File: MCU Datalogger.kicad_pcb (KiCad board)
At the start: 2 copper layers, 51.4 x 34.3 mm, 31 parts, among them J1 Conn_01x04_Male, J2 Conn_01x09_Male, J3 Conn_01x04_Male, J4 Conn_02x03_Odd_Even, U1 24LC1025, U2 DS1337S+, U3 24LC1025, U4 ATMEGA328P-AU, Y1 32.768 KHz, Y2 16 MHz

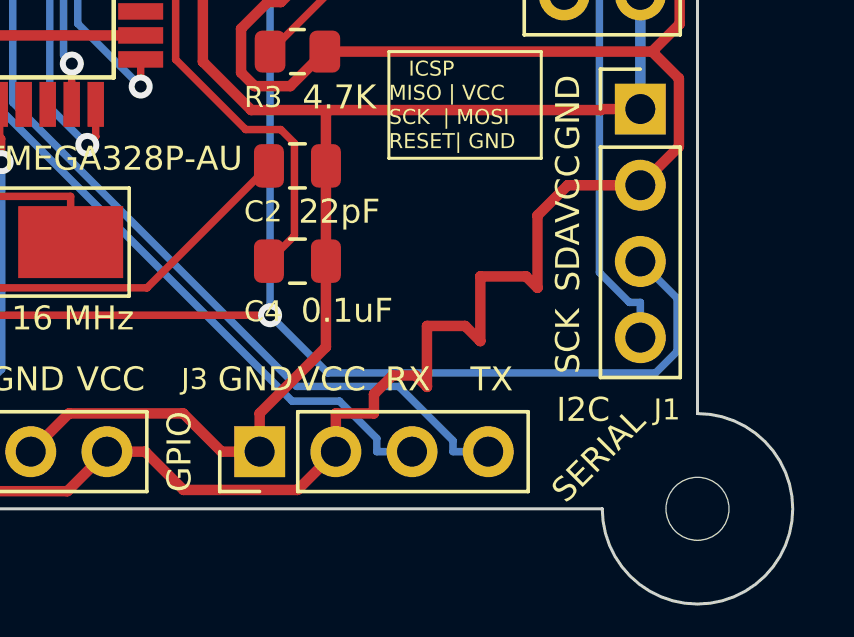
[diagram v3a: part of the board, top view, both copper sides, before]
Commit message: Changes due to various feature demos.
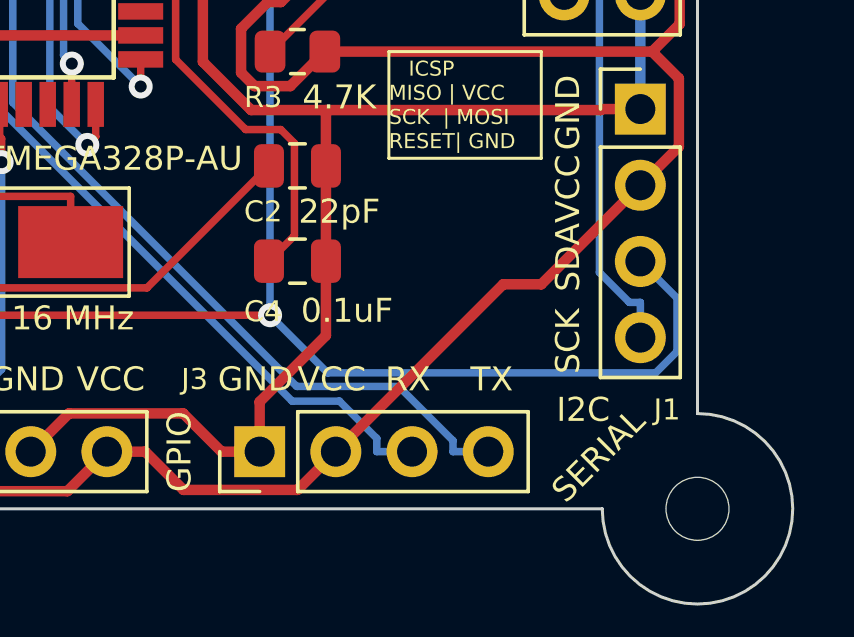
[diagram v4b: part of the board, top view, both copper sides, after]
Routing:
- net /Vcc: track 189.0 -> 182.9 mm
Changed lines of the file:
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@@
   (segment (start 111.9753 84.69) (end 117.4247 84.69) (width 0.35) (layer "F.Cu") (net 1))
   (segment (start 107.6152 85.49) (end 110 85.49) (width 0.35) (layer "F.Cu") (net 1))
-  (segment (start 124.775 94.615) (end 124.775 97.4797) (width 0.35) (layer "F.Cu") (net 1))
   (segment (start 110.7217 76.7517) (end 111.3752 76.7517) (width 0.35) (layer "F.Cu") (net 1))
   (segment (start 114.935 100.965) (end 116.2103 99.6897) (width 0.35) (layer "F.Cu") (net 1))
@@
   (segment (start 123.5904 81.1571) (end 124.7375 80.01) (width 0.35) (layer "F.Cu") (net 1))
   (segment (start 119.695 77.8868) (end 119.695 78.5117) (width 0.35) (layer "F.Cu") (net 1))
+  (segment (start 124.775 97.094) (end 124.775 94.615) (width 0.35) (layer "F.Cu") (net 1))
   (segment (start 133.9454 89.5793) (end 124.775 89.5793) (width 0.35) (layer "F.Cu") (net 1))
   (segment (start 106.7068 84.5816) (end 105.3266 84.5816) (width 0.35) (layer "F.Cu") (net 1))
@@
   (segment (start 118.6 84.69) (end 119.7753 84.69) (width 0.35) (layer "F.Cu") (net 1))
   (segment (start 99.3951 78.0591) (end 98.806 77.47) (width 0.35) (layer "F.Cu") (net 1))
-  (segment (start 122.565 100.965) (end 122.565 99.6897) (width 0.35) (layer "F.Cu") (net 1))
   (segment (start 110 83.89) (end 111.1753 83.89) (width 0.35) (layer "F.Cu") (net 1))
+  (segment (start 122.565 100.965) (end 122.565 99.304) (width 0.35) (layer "F.Cu") (net 1))
   (segment (start 93.98 85.085) (end 95.2553 85.085) (width 0.35) (layer "F.Cu") (net 1))
   (segment (start 116.2103 99.6897) (end 120.0144 99.6897) (width 0.35) (layer "F.Cu") (net 1))
-  (segment (start 124.775 97.4797) (end 122.565 99.6897) (width 0.35) (layer "F.Cu") (net 1))
   (segment (start 100.1112 77.47) (end 105.2 77.47) (width 0.35) (layer "F.Cu") (net 1))
   (segment (start 119.695 76.2) (end 119.695 77.8868) (width 0.35) (layer "F.Cu") (net 1))
@@
   (segment (start 119.695 78.5117) (end 122.3404 81.1571) (width 0.35) (layer "F.Cu") (net 1))
   (segment (start 118.6 84.69) (end 117.4247 84.69) (width 0.35) (layer "F.Cu") (net 1))
+  (segment (start 122.565 99.304) (end 124.775 97.094) (width 0.35) (layer "F.Cu") (net 1))
   (segment (start 111.9269 76.2) (end 111.3752 76.7517) (width 0.35) (layer "F.Cu") (net 1))
   (segment (start 120.0144 99.6897) (end 121.2897 100.965) (width 0.35) (layer "F.Cu") (net 1))
@@
   (segment (start 128.5013 77.8868) (end 129.1825 78.568) (width 0.35) (layer "B.Cu") (net 1))
   (segment (start 93.98 82.545) (end 93.98 81.2697) (width 0.35) (layer "F.Cu") (net 2))
+  (segment (start 130.683 95.387) (end 131.953 95.387) (width 0.35) (layer "F.Cu") (net 2))
   (segment (start 105.2271 82.1769) (end 105.2271 83.1579) (width 0.35) (layer "F.Cu") (net 2))
   (segment (start 122.3954 88.7808) (end 121.9446 88.33) (width 0.35) (layer "F.Cu") (net 2))
@@
   (segment (start 124.7375 84.514) (end 124.7375 83.82) (width 0.35) (layer "F.Cu") (net 2))
   (segment (start 122.3831 82.0941) (end 123.0116 82.0941) (width 0.35) (layer "F.Cu") (net 2))
-  (segment (start 131.826 93.091) (end 132.832 92.085) (width 0.35) (layer "F.Cu") (net 2))
   (segment (start 105.2271 83.1579) (end 105.2 83.185) (width 0.35) (layer "F.Cu") (net 2))
-  (segment (start 127 98.425) (end 127.762 98.425) (width 0.35) (layer "F.Cu") (net 2))
-  (segment (start 128.143 98.806) (end 128.143 96.774) (width 0.35) (layer "F.Cu") (net 2))
   (segment (start 98 83.185) (end 95.8953 83.185) (width 0.35) (layer "F.Cu") (net 2))
   (segment (start 120.0257 102.2404) (end 123.8296 102.2404) (width 0.35) (layer "F.Cu") (net 2))
   (segment (start 103.2872 97.6503) (end 104.4175 96.52) (width 0.35) (layer "F.Cu") (net 2))
   (segment (start 98 85.725) (end 98 84.455) (width 0.35) (layer "F.Cu") (net 2))
-  (segment (start 128.143 96.774) (end 129.413 96.774) (width 0.35) (layer "F.Cu") (net 2))
   (segment (start 101.6 91.2347) (end 102.6647 90.17) (width 0.35) (layer "F.Cu") (net 2))
   (segment (start 124.7375 87.63) (end 123.5867 88.7808) (width 0.35) (layer "F.Cu") (net 2))
   (segment (start 102.6647 89.9899) (end 98.3998 85.725) (width 0.35) (layer "F.Cu") (net 2))
   (segment (start 118.7503 100.965) (end 120.0257 102.2404) (width 0.35) (layer "F.Cu") (net 2))
+  (segment (start 131.953 95.387) (end 135.255 92.085) (width 0.35) (layer "F.Cu") (net 2))
   (segment (start 97.645 76.2) (end 98 76.2) (width 0.35) (layer "F.Cu") (net 2))
   (segment (start 125.7262 80.6987) (end 125.7262 77.1637) (width 0.35) (layer "F.Cu") (net 2))
@@
   (segment (start 95.8403 99.9486) (end 95.8403 102.032) (width 0.35) (layer "F.Cu") (net 2))
   (segment (start 136.5396 90.8004) (end 136.5396 88.5225) (width 0.35) (layer "F.Cu") (net 2))
-  (segment (start 127.762 98.425) (end 128.143 98.806) (width 0.35) (layer "F.Cu") (net 2))
-  (segment (start 126.375 99.6897) (end 126.375 99.05) (width 0.35) (layer "F.Cu") (net 2))
   (segment (start 95.8403 102.032) (end 96.0919 102.2836) (width 0.35) (layer "F.Cu") (net 2))
   (segment (start 96.0919 102.2836) (end 116.1564 102.2836) (width 0.35) (layer "F.Cu") (net 2))
@@
   (segment (start 136.566 81.971) (end 136.566 86.7111) (width 0.35) (layer "F.Cu") (net 2))
   (segment (start 117.795 76.2) (end 117.795 77.506) (width 0.35) (layer "F.Cu") (net 2))
-  (segment (start 129.921 95.123) (end 131.445 95.123) (width 0.35) (layer "F.Cu") (net 2))
-  (segment (start 132.832 92.085) (end 135.255 92.085) (width 0.35) (layer "F.Cu") (net 2))
   (segment (start 106.5848 83.185) (end 108.0898 84.69) (width 0.35) (layer "F.Cu") (net 2))
   (segment (start 96.7226 78.74) (end 96.5097 78.74) (width 0.35) (layer "F.Cu") (net 2))
-  (segment (start 125.105 99.6897) (end 126.375 99.6897) (width 0.35) (layer "F.Cu") (net 2))
   (segment (start 101.6 97.6503) (end 101.6 91.2347) (width 0.35) (layer "F.Cu") (net 2))
   (segment (start 123.6712 82.7537) (end 124.7375 83.82) (width 0.35) (layer "F.Cu") (net 2))
+  (segment (start 125.105 100.965) (end 130.683 95.387) (width 0.35) (layer "F.Cu") (net 2))
   (segment (start 122.8345 85.9791) (end 123.2724 85.9791) (width 0.35) (layer "F.Cu") (net 2))
   (segment (start 102.6647 90.17) (end 102.6647 89.9899) (width 0.35) (layer "F.Cu") (net 2))
   (segment (start 127.3575 83.82) (end 124.7375 83.82) (width 0.35) (layer "F.Cu") (net 2))
-  (segment (start 129.413 96.774) (end 129.921 97.282) (width 0.35) (layer "F.Cu") (net 2))
   (segment (start 123.6712 82.7537) (end 125.7262 80.6987) (width 0.35) (layer "F.Cu") (net 2))
   (segment (start 98 84.455) (end 98 83.185) (width 0.35) (layer "F.Cu") (net 2))
-  (segment (start 131.445 95.123) (end 131.826 95.504) (width 0.35) (layer "F.Cu") (net 2))
   (segment (start 98.1427 97.6462) (end 95.8403 99.9486) (width 0.35) (layer "F.Cu") (net 2))
   (segment (start 95.8953 83.185) (end 95.2553 82.545) (width 0.35) (layer "F.Cu") (net 2))
   (segment (start 108.27 76.2) (end 105.2 76.2) (width 0.35) (layer "F.Cu") (net 2))
-  (segment (start 129.921 97.282) (end 129.921 95.123) (width 0.35) (layer "F.Cu") (net 2))
   (segment (start 117.795 77.506) (end 122.3831 82.0941) (width 0.35) (layer "F.Cu") (net 2))
   (segment (start 116.1564 102.2836) (end 117.475 100.965) (width 0.35) (layer "F.Cu") (net 2))
@@
   (segment (start 118.6 87.09) (end 113.246 87.09) (width 0.35) (layer "F.Cu") (net 2))
   (segment (start 123.2724 85.9791) (end 124.7375 84.514) (width 0.35) (layer "F.Cu") (net 2))
-  (segment (start 131.826 95.504) (end 131.826 93.091) (width 0.35) (layer "F.Cu") (net 2))
   (segment (start 135.255 92.085) (end 136.5396 90.8004) (width 0.35) (layer "F.Cu") (net 2))
   (segment (start 123.8296 102.2404) (end 125.105 100.965) (width 0.35) (layer "F.Cu") (net 2))
@@
   (segment (start 104.075 90.17) (end 102.6647 90.17) (width 0.35) (layer "F.Cu") (net 2))
   (segment (start 98.7825 96.52) (end 98.7825 97.6462) (width 0.35) (layer "F.Cu") (net 2))
-  (segment (start 126.375 99.05) (end 127 98.425) (width 0.35) (layer "F.Cu") (net 2))
   (segment (start 98.3998 85.725) (end 98 85.725) (width 0.35) (layer "F.Cu") (net 2))
-  (segment (start 125.105 100.965) (end 125.105 99.6897) (width 0.35) (layer "F.Cu") (net 2))
   (segment (start 96.7226 77.1224) (end 97.645 76.2) (width 0.35) (layer "F.Cu") (net 2))
   (segment (start 123.0116 82.0941) (end 123.6712 82.7537) (width 0.35) (layer "F.Cu") (net 2))

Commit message: Added custom graphics.
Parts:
- added G***: LOGO, Footprints:TE_Logo_10mm_negative_silkscreen, B.Cu at (101.7, 92.5)
